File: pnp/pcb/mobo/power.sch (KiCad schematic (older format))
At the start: 26 parts, among them J45 Jack-DC, U5 AP1117-33, U7 TPS54336ADDA

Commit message: added reverse polarity protection with a p channel fet
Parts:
- added Q?: FDS4435BZ, SO08-E3, symbol FDS4435BZ:FDS4435BZ
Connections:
- wire segments 54 -> 56
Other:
- moved on the sheet: C10, C11, C12, C13, C29, C30, C31, C7, C8, C9, D1, D2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

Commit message: assigned a footprint to the instrumentation amplifier, deleted all traces from old layout
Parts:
- gave numbers to parts that had none: 1
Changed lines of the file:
@@
 $EndComp
 $Comp
-L FDS4435BZ:FDS4435BZ Q?
+L FDS4435BZ:FDS4435BZ Q5
 U 1 1 5F859F89
 P 2825 1750
-F 0 "Q?" V 3060 1750 50  0000 C CNN
+F 0 "Q5" V 3060 1750 50  0000 C CNN
 F 1 "FDS4435BZ" V 2969 1750 50  0000 C CNN
 F 2 "SO08-E3" H 2825 1750 50  0001 L BNN
@@
 $EndComp
 $Comp
-L power:GND #PWR?
+L power:GND #PWR0222
 U 1 1 5F8673FB
 P 2300 1950
-F 0 "#PWR?" H 2300 1700 50  0001 C CNN
+F 0 "#PWR0222" H 2300 1700 50  0001 C CNN
 F 1 "GND" H 2305 1777 50  0000 C CNN
 F 2 "" H 2300 1950 50  0001 C CNN

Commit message: added in custom symbols for most parts in vacuum circuit, rewired it with those symbols, redid footprint allocation for the board. ready for layout
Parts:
- removed Q5: FDS4435BZ, SO08-E3, symbol FDS4435BZ:FDS4435BZ
- added U14: FDS4435BZ, Package_SO:SO-8_3.9x4.9mm_P1.27mm, symbol index:FDS4435BZ
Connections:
- wire segments 56 -> 70
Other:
- moved on the sheet: J45
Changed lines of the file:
@@
 L Connector:Jack-DC J?
 U 1 1 5EB1A37C
-P 2000 1850
+P 1550 1850
 AR Path="/5EB1A37C" Ref="J?"  Part="1"
 AR Path="/5EB15D5B/5EB1A37C" Ref="J45"  Part="1"
-F 0 "J45" H 2057 2175 50  0000 C CNN
-F 1 "Jack-DC" H 2057 2084 50  0000 C CNN
-F 2 "Connector_BarrelJack:BarrelJack_Horizontal" H 2050 1810 50  0001 C CNN
-F 3 "~" H 2050 1810 50  0001 C CNN
-	1    2000 1850
+F 0 "J45" H 1607 2175 50  0000 C CNN
+F 1 "Jack-DC" H 1607 2084 50  0000 C CNN
+F 2 "Connector_BarrelJack:BarrelJack_Horizontal" H 1600 1810 50  0001 C CNN
+F 3 "~" H 1600 1810 50  0001 C CNN
+	1    1550 1850
 	1    0    0    -1
 $EndComp
@@
 Text Notes 5525 3275 0    50   ~ 0
 3V3 LDO
-Text Notes 2850 1375 0    50   ~ 0
+Text Notes 1900 1050 0    50   ~ 0
 12V In
 $Comp
@@
 $EndComp
 $Comp
-L FDS4435BZ:FDS4435BZ Q5
-U 1 1 5F859F89
-P 2825 1750
-F 0 "Q5" V 3060 1750 50  0000 C CNN
-F 1 "FDS4435BZ" V 2969 1750 50  0000 C CNN
-F 2 "SO08-E3" H 2825 1750 50  0001 L BNN
-F 3 "" H 2825 1750 50  0001 C CNN
-	1    2825 1750
-	0    -1   -1   0
-$EndComp
-$Comp
 L power:GND #PWR0222
 U 1 1 5F8673FB
-P 2300 1950
-F 0 "#PWR0222" H 2300 1700 50  0001 C CNN
-F 1 "GND" H 2305 1777 50  0000 C CNN
-F 2 "" H 2300 1950 50  0001 C CNN
-F 3 "" H 2300 1950 50  0001 C CNN
-	1    2300 1950
-	1    0    0    -1
-$EndComp
-Wire Wire Line
-	2300 1750 2625 1750
-Wire Wire Line
-	3025 1750 3450 1750
+P 1850 1950
+F 0 "#PWR0222" H 1850 1700 50  0001 C CNN
+F 1 "GND" H 1855 1777 50  0000 C CNN
+F 2 "" H 1850 1950 50  0001 C CNN
+F 3 "" H 1850 1950 50  0001 C CNN
+	1    1850 1950
+	1    0    0    -1
+$EndComp
 Connection ~ 3450 1750
 Wire Wire Line
-	2300 1950 2925 1950
-Connection ~ 2300 1950
-Wire Wire Line
-	2925 1950 3150 1950
-Wire Wire Line
 	3150 1950 3150 2050
 Wire Wire Line
 	3150 2050 3450 2050
-Connection ~ 2925 1950
 Connection ~ 3450 2050
+$Comp
+L index:FDS4435BZ U14
+U 1 1 5FB00382
+P 2500 1600
+F 0 "U14" H 2500 1185 50  0000 C CNN
+F 1 "FDS4435BZ" H 2500 1276 50  0000 C CNN
+F 2 "Package_SO:SO-8_3.9x4.9mm_P1.27mm" H 2500 1600 50  0001 C CNN
+F 3 "" H 2500 1600 50  0001 C CNN
+	1    2500 1600
+	-1   0    0    1
+$EndComp
+Wire Wire Line
+	2850 1550 2900 1550
+Wire Wire Line
+	2900 1550 2900 1650
+Wire Wire Line
+	2900 1750 2850 1750
+Connection ~ 2900 1750
+Wire Wire Line
+	2900 1750 3450 1750
+Wire Wire Line
+	2850 1650 2900 1650
+Connection ~ 2900 1650
+Wire Wire Line
+	2900 1650 2900 1750
+Wire Wire Line
+	2150 1450 2100 1450
+Wire Wire Line
+	2100 1450 2100 1550
+Wire Wire Line
+	2100 1750 2150 1750
+Wire Wire Line
+	2150 1650 2100 1650
+Connection ~ 2100 1650
+Wire Wire Line
+	2100 1650 2100 1750
+Wire Wire Line
+	2100 1550 2150 1550
+Connection ~ 2100 1550
+Wire Wire Line
+	2100 1550 2100 1650
+Wire Wire Line
+	2100 1750 1850 1750
+Connection ~ 2100 1750
+Wire Wire Line
+	2850 1450 3000 1450
+Wire Wire Line
+	3000 1450 3000 1950
+Connection ~ 3000 1950
+Wire Wire Line
+	3000 1950 3150 1950
+Wire Wire Line
+	1850 1950 3000 1950
+Connection ~ 1850 1950
 $EndSCHEMATC

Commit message: switched to two 10-pin aux ports
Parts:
- U14: symbol index:FDS4435BZ -> mobo-rescue:FDS4435BZ-index
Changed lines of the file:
@@
 Connection ~ 3450 2050
 $Comp
-L index:FDS4435BZ U14
+L mobo-rescue:FDS4435BZ-index U14
 U 1 1 5FB00382
 P 2500 1600

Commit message: Deleted rescue lib and fixed components library reference
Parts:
- U14: symbol mobo-rescue:FDS4435BZ-index -> index:FDS4435BZ
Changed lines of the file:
@@
 Connection ~ 3450 2050
 $Comp
-L mobo-rescue:FDS4435BZ-index U14
+L index:FDS4435BZ U14
 U 1 1 5FB00382
 P 2500 1600

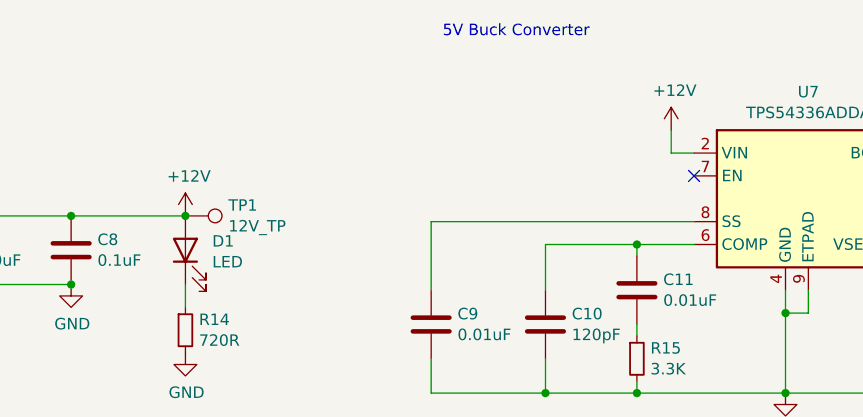
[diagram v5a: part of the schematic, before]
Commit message: Add 24VDC support
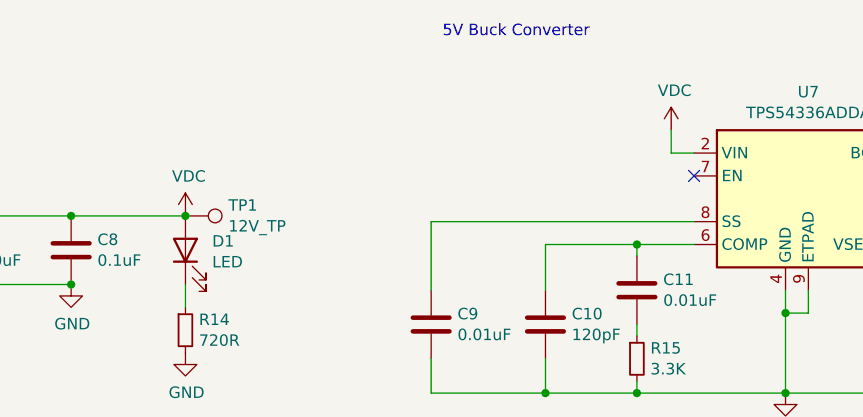
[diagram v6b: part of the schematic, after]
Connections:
- net +12V renamed VDC
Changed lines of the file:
@@
-$EndComp
-$Comp
-L power:+12V #PWR0249
-U 1 1 5EB1C14F
-P 4500 1750
-F 0 "#PWR0249" H 4500 1600 50  0001 C CNN
-F 1 "+12V" H 4515 1923 50  0000 C CNN
-F 2 "" H 4500 1750 50  0001 C CNN
-F 3 "" H 4500 1750 50  0001 C CNN
-	1    4500 1750
-	1    0    0    -1
 $EndComp
 $Comp
@@
 	4000 1750 3450 1750
 Connection ~ 4000 2050
-$Comp
-L power:+12V #PWR0250
-U 1 1 5EB22049
-P 6625 1375
-F 0 "#PWR0250" H 6625 1225 50  0001 C CNN
-F 1 "+12V" H 6640 1548 50  0000 C CNN
-F 2 "" H 6625 1375 50  0001 C CNN
-F 3 "" H 6625 1375 50  0001 C CNN
-	1    6625 1375
-	1    0    0    -1
-$EndComp
 $Comp
 L pspice:INDUCTOR L1
@@
 	1850 1950 3000 1950
 Connection ~ 1850 1950
+$Comp
+L power:VDC #PWR015
+U 1 1 5FE000FB
+P 4500 1750
+F 0 "#PWR015" H 4500 1650 50  0001 C CNN
+F 1 "VDC" H 4515 1923 50  0000 C CNN
+F 2 "" H 4500 1750 50  0001 C CNN
+F 3 "" H 4500 1750 50  0001 C CNN
+	1    4500 1750
+	1    0    0    -1
+$EndComp
+$Comp
+L power:VDC #PWR016
+U 1 1 5FE01528
+P 6625 1375
+F 0 "#PWR016" H 6625 1275 50  0001 C CNN
+F 1 "VDC" H 6640 1548 50  0000 C CNN
+F 2 "" H 6625 1375 50  0001 C CNN
+F 3 "" H 6625 1375 50  0001 C CNN
+	1    6625 1375
+	1    0    0    -1
+$EndComp
 $EndSCHEMATC

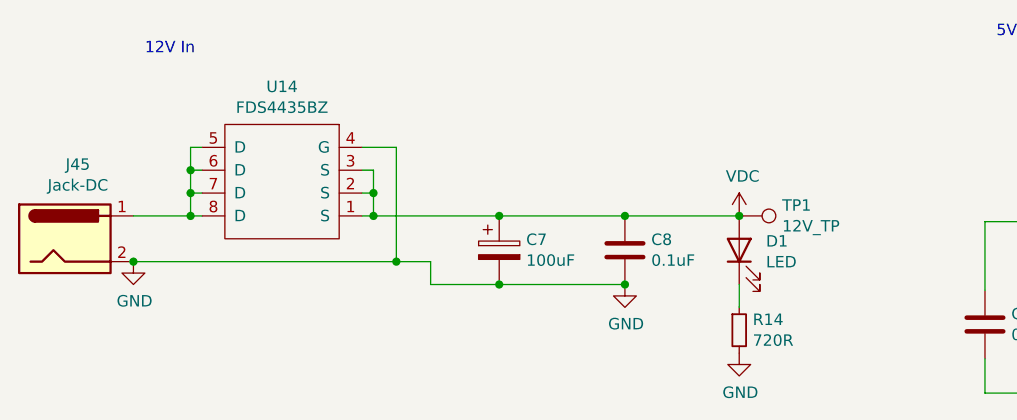
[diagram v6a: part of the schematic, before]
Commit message: Replace MOSFETs and organized vacuum sensor
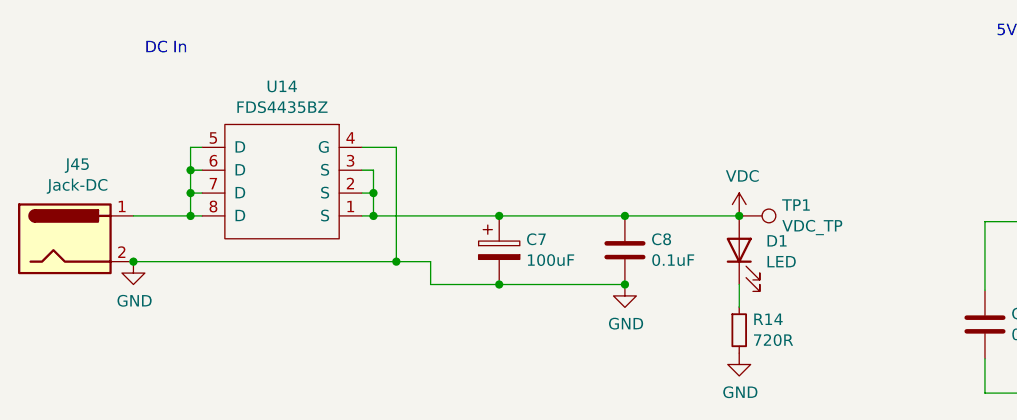
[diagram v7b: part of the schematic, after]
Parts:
- R14, R15, R16, R17, R18, R42: footprint Resistor_SMD:R_0805_2012Metric_Pad1.15x1.40mm_HandSolder -> Resistor_SMD:R_0805_2012Metric_Pad1.20x1.40mm_HandSolder
- TP1: value 12V_TP -> VDC_TP
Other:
- note added: "DC In"
- note removed: "12V In"
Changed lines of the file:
@@
 $Descr A4 11693 8268
 encoding utf-8
-Sheet 6 6
+Sheet 8 8
 Title ""
 Date ""
@@
 F 0 "R15" H 6534 2421 50  0000 L CNN
 F 1 "3.3K" H 6534 2330 50  0000 L CNN
-F 2 "Resistor_SMD:R_0805_2012Metric_Pad1.15x1.40mm_HandSolder" H 6475 2375 50  0001 C CNN
+F 2 "Resistor_SMD:R_0805_2012Metric_Pad1.20x1.40mm_HandSolder" H 6475 2375 50  0001 C CNN
 F 3 "~" H 6475 2375 50  0001 C CNN
 	1    6475 2375
@@
 F 0 "R42" H 10134 2321 50  0000 L CNN
 F 1 "470R" H 10134 2230 50  0000 L CNN
-F 2 "Resistor_SMD:R_0805_2012Metric_Pad1.15x1.40mm_HandSolder" H 10075 2275 50  0001 C CNN
+F 2 "Resistor_SMD:R_0805_2012Metric_Pad1.20x1.40mm_HandSolder" H 10075 2275 50  0001 C CNN
 F 3 "~" H 10075 2275 50  0001 C CNN
 	1    10075 2275
@@
 F 0 "R17" H 9634 2471 50  0000 L CNN
 F 1 "2.7K" H 9634 2380 50  0000 L CNN
-F 2 "Resistor_SMD:R_0805_2012Metric_Pad1.15x1.40mm_HandSolder" H 9575 2425 50  0001 C CNN
+F 2 "Resistor_SMD:R_0805_2012Metric_Pad1.20x1.40mm_HandSolder" H 9575 2425 50  0001 C CNN
 F 3 "~" H 9575 2425 50  0001 C CNN
 	1    9575 2425
@@
 F 0 "R16" H 9634 2171 50  0000 L CNN
 F 1 "15K" H 9634 2080 50  0000 L CNN
-F 2 "Resistor_SMD:R_0805_2012Metric_Pad1.15x1.40mm_HandSolder" H 9575 2125 50  0001 C CNN
+F 2 "Resistor_SMD:R_0805_2012Metric_Pad1.20x1.40mm_HandSolder" H 9575 2125 50  0001 C CNN
 F 3 "~" H 9575 2125 50  0001 C CNN
 	1    9575 2125
@@
 3V3 LDO
 Text Notes 1900 1050 0    50   ~ 0
-12V In
+DC In
 $Comp
 L power:+5V #PWR0185
@@
 P 4500 1750
 F 0 "TP1" V 4454 1938 50  0000 L CNN
-F 1 "12V_TP" V 4545 1938 50  0000 L CNN
+F 1 "VDC_TP" V 4545 1938 50  0000 L CNN
 F 2 "TestPoint:TestPoint_THTPad_1.0x1.0mm_Drill0.5mm" H 4700 1750 50  0001 C CNN
 F 3 "~" H 4700 1750 50  0001 C CNN
@@
 F 0 "R18" H 7709 4246 50  0000 L CNN
 F 1 "180R" H 7709 4155 50  0000 L CNN
-F 2 "Resistor_SMD:R_0805_2012Metric_Pad1.15x1.40mm_HandSolder" H 7650 4200 50  0001 C CNN
+F 2 "Resistor_SMD:R_0805_2012Metric_Pad1.20x1.40mm_HandSolder" H 7650 4200 50  0001 C CNN
 F 3 "~" H 7650 4200 50  0001 C CNN
 	1    7650 4200
@@
 F 0 "R14" H 4559 2296 50  0000 L CNN
 F 1 "720R" H 4559 2205 50  0000 L CNN
-F 2 "Resistor_SMD:R_0805_2012Metric_Pad1.15x1.40mm_HandSolder" H 4500 2250 50  0001 C CNN
+F 2 "Resistor_SMD:R_0805_2012Metric_Pad1.20x1.40mm_HandSolder" H 4500 2250 50  0001 C CNN
 F 3 "~" H 4500 2250 50  0001 C CNN
 	1    4500 2250

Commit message: Revert "Replace MOSFETs and organized vacuum sensor"
This reverts commit d845c98ea56ba571b636da2743323a7f663cddfe.
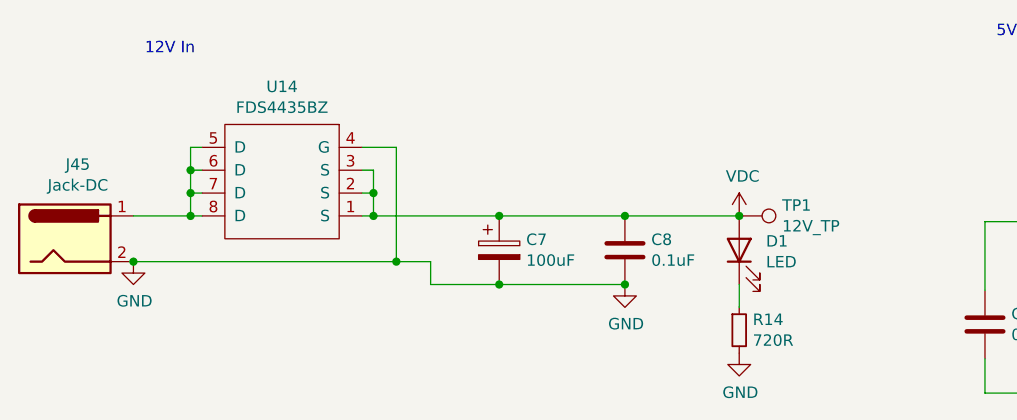
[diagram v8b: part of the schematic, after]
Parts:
- R14, R15, R16, R17, R18, R42: footprint Resistor_SMD:R_0805_2012Metric_Pad1.20x1.40mm_HandSolder -> Resistor_SMD:R_0805_2012Metric_Pad1.15x1.40mm_HandSolder
- TP1: value VDC_TP -> 12V_TP
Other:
- note added: "12V In"
- note removed: "DC In"
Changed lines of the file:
@@
 $Descr A4 11693 8268
 encoding utf-8
-Sheet 8 8
+Sheet 6 6
 Title ""
 Date ""
@@
 F 0 "R15" H 6534 2421 50  0000 L CNN
 F 1 "3.3K" H 6534 2330 50  0000 L CNN
-F 2 "Resistor_SMD:R_0805_2012Metric_Pad1.20x1.40mm_HandSolder" H 6475 2375 50  0001 C CNN
+F 2 "Resistor_SMD:R_0805_2012Metric_Pad1.15x1.40mm_HandSolder" H 6475 2375 50  0001 C CNN
 F 3 "~" H 6475 2375 50  0001 C CNN
 	1    6475 2375
@@
 F 0 "R42" H 10134 2321 50  0000 L CNN
 F 1 "470R" H 10134 2230 50  0000 L CNN
-F 2 "Resistor_SMD:R_0805_2012Metric_Pad1.20x1.40mm_HandSolder" H 10075 2275 50  0001 C CNN
+F 2 "Resistor_SMD:R_0805_2012Metric_Pad1.15x1.40mm_HandSolder" H 10075 2275 50  0001 C CNN
 F 3 "~" H 10075 2275 50  0001 C CNN
 	1    10075 2275
@@
 F 0 "R17" H 9634 2471 50  0000 L CNN
 F 1 "2.7K" H 9634 2380 50  0000 L CNN
-F 2 "Resistor_SMD:R_0805_2012Metric_Pad1.20x1.40mm_HandSolder" H 9575 2425 50  0001 C CNN
+F 2 "Resistor_SMD:R_0805_2012Metric_Pad1.15x1.40mm_HandSolder" H 9575 2425 50  0001 C CNN
 F 3 "~" H 9575 2425 50  0001 C CNN
 	1    9575 2425
@@
 F 0 "R16" H 9634 2171 50  0000 L CNN
 F 1 "15K" H 9634 2080 50  0000 L CNN
-F 2 "Resistor_SMD:R_0805_2012Metric_Pad1.20x1.40mm_HandSolder" H 9575 2125 50  0001 C CNN
+F 2 "Resistor_SMD:R_0805_2012Metric_Pad1.15x1.40mm_HandSolder" H 9575 2125 50  0001 C CNN
 F 3 "~" H 9575 2125 50  0001 C CNN
 	1    9575 2125
@@
 3V3 LDO
 Text Notes 1900 1050 0    50   ~ 0
-DC In
+12V In
 $Comp
 L power:+5V #PWR0185
@@
 P 4500 1750
 F 0 "TP1" V 4454 1938 50  0000 L CNN
-F 1 "VDC_TP" V 4545 1938 50  0000 L CNN
+F 1 "12V_TP" V 4545 1938 50  0000 L CNN
 F 2 "TestPoint:TestPoint_THTPad_1.0x1.0mm_Drill0.5mm" H 4700 1750 50  0001 C CNN
 F 3 "~" H 4700 1750 50  0001 C CNN
@@
 F 0 "R18" H 7709 4246 50  0000 L CNN
 F 1 "180R" H 7709 4155 50  0000 L CNN
-F 2 "Resistor_SMD:R_0805_2012Metric_Pad1.20x1.40mm_HandSolder" H 7650 4200 50  0001 C CNN
+F 2 "Resistor_SMD:R_0805_2012Metric_Pad1.15x1.40mm_HandSolder" H 7650 4200 50  0001 C CNN
 F 3 "~" H 7650 4200 50  0001 C CNN
 	1    7650 4200
@@
 F 0 "R14" H 4559 2296 50  0000 L CNN
 F 1 "720R" H 4559 2205 50  0000 L CNN
-F 2 "Resistor_SMD:R_0805_2012Metric_Pad1.20x1.40mm_HandSolder" H 4500 2250 50  0001 C CNN
+F 2 "Resistor_SMD:R_0805_2012Metric_Pad1.15x1.40mm_HandSolder" H 4500 2250 50  0001 C CNN
 F 3 "~" H 4500 2250 50  0001 C CNN
 	1    4500 2250
